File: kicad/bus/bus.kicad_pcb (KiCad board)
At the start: 2 copper layers, 45 parts, among them J1 Barrel_Jack, U29 L7805

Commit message: stuff
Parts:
- removed R12: 1k, Resistor_THT:R_Axial_DIN0207_L6.3mm_D2.5mm_P7.62mm_Horizontal
- added R14: 1k, custom_footprint_library:0.4_pitch_resistor, F.Cu at (270.5, 76.2)
- added U32: ~, custom_footprint_library:jumper, F.Cu at (133.8, 128.3)
- added U33: ~, custom_footprint_library:jumper, F.Cu at (133.8, 137.2)
- added U34: ~, Connector_PinHeader_2.54mm:PinHeader_1x07_P2.54mm_Vertical, F.Cu at (116.4, 122.4)
- R1, R10, R11, R13, R2, R3, R4, R5, R6, R7, R8, R9: footprint Resistor_THT:R_Axial_DIN0207_L6.3mm_D2.5mm_P7.62mm_Horizontal -> custom_footprint_library:0.4_pitch_resistor
- U1: footprint Connector_PinHeader_2.54mm:PinHeader_1x10_P2.54mm_Vertical -> Connector_PinHeader_2.54mm:PinHeader_1x11_P2.54mm_Vertical
- U2, U24, U3, U4, U5, U6, U7: footprint Connector_PinHeader_2.54mm:PinHeader_1x22_P2.54mm_Vertical -> Connector_PinHeader_2.54mm:PinHeader_1x23_P2.54mm_Vertical
- moved U2 152.6 mm to (259.1, 134.6), turned to 180 degrees
- moved U24 142.1 mm to (275.6, 134.6), turned to 180 degrees
- moved U3 133.1 mm to (242.6, 134.6), turned to 180 degrees
- moved U4 114.4 mm to (226.1, 134.6), turned to 180 degrees
- moved U5 96.5 mm to (209.6, 134.6), turned to 180 degrees
- moved U6 80.4 mm to (193.0, 134.6), turned to 180 degrees
- moved U7 67.0 mm to (176.5, 134.6), turned to 180 degrees
- moved R13 65.5 mm to (270.5, 109.2)
- moved R11 64.3 mm to (254.0, 76.2), turned to 180 degrees
- moved U1 48.5 mm to (102.5, 90.3)
- moved U11 48.5 mm to (112.6, 68.1)
- moved U25 48.5 mm to (108.2, 48.7)
- moved U28 48.5 mm to (119.1, 48.7)
- moved U9 48.5 mm to (64.8, 48.7)
- moved U8 48.5 mm to (54.0, 48.7)
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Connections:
- U16 pad 4: Net-(U10-GND) -> Net-(U16-2A)
- U16 pad 5: Net-(U10-GND) -> Net-(U16-2B)
- U16 pad 6: unconnected-(U16-2Q-Pad6) -> Net-(U16-2Q)
- U20 pad 1: Net-(U20-IN) -> Net-(U16-2Q)
- U21 pad 1: Net-(U19-IN) -> Net-(U21-IN)
- U28 pad 13: Net-(U19-IN) -> Net-(U21-IN)
- U30 pad 4: Net-(U10-GND) -> Net-(U21-IN)
- U30 pad 5: Net-(U10-GND) -> Net-(U16-2B)
- U30 pad 6: unconnected-(U30-2Q-Pad6) -> Net-(U19-IN)
- U31 pad 1: Net-(U20-IN) -> Net-(U16-2A)
- U31 pad 9: Net-(U19-IN) -> Net-(U21-IN)
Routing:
- net Net-(U10-GND): track 0.00 -> 203.2 mm
- net Net-(U15-D5): track 0.00 -> 128.3 mm
- net Net-(U15-D3): track 0.00 -> 128.3 mm
- net Net-(U15-D7): track 0.00 -> 128.3 mm
- net Net-(U15-D6): track 0.00 -> 128.3 mm
- net Net-(U15-D4): track 0.00 -> 128.3 mm
- net Net-(U15-D2): track 0.00 -> 128.3 mm
- net Net-(U15-D1): track 0.00 -> 128.3 mm
- net Net-(U15-D0): track 0.00 -> 128.3 mm
- net Net-(U16-2B): track 0.00 -> 99.1 mm
- net Net-(U7-FAULT): track 0.00 -> 5.08 mm
- net Net-(U4-FAULT): track 0.00 -> 5.08 mm
- net Net-(U6-FAULT): track 0.00 -> 5.08 mm
- net Net-(U3-FAULT): track 0.00 -> 5.08 mm
- net Net-(U24-FAULT): track 0.00 -> 5.08 mm
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
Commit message: Finished main PCB design
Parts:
- moved U9 122.8 mm to (187.6, 48.9), turned to 90 degrees
- moved U8 115.7 mm to (169.2, 38.1)
- moved U10 112.3 mm to (183.9, 144.8), turned to 90 degrees
- moved U25 107.3 mm to (215.0, 38.1)
- moved U13 106.3 mm to (208.0, 144.8), turned to 90 degrees
- moved U14 90.9 mm to (75.3, 139.7), turned to 180 degrees
- moved U31 90.9 mm to (75.3, 111.7), turned to 180 degrees
- moved U11 90.0 mm to (159.7, 144.8), turned to 90 degrees
- moved U33 84.0 mm to (94.9, 62.8)
- moved U32 82.9 mm to (94.9, 55.0)
- moved U34 82.6 mm to (95.2, 42.5), turned to 90 degrees
- moved U12 77.6 mm to (135.6, 144.8), turned to 90 degrees
- moved R4 69.3 mm to (119.1, 101.6)
- moved U30 62.7 mm to (67.6, 41.2)
- moved U28 56.1 mm to (75.3, 83.8), turned to 180 degrees
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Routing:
- net Net-(U10-GND): track 203.2 -> 822.5 mm
- net Net-(U10-E1): track 0.00 -> 588.7 mm, vias 0 -> 2
- net Net-(U14-0CLK): track 0.00 -> 293.3 mm, vias 0 -> 1
- net Net-(U14-1Q): track 0.00 -> 239.4 mm
- net Net-(U2-CLK_B): track 0.00 -> 218.6 mm, vias 0 -> 1
- net Net-(U12-E2#): track 0.00 -> 193.9 mm, vias 0 -> 1
- net Net-(U31-0CLK): track 0.00 -> 182.8 mm, vias 0 -> 1
- net Net-(U26-IN): track 0.00 -> 148.6 mm, vias 0 -> 2
- net Net-(U34-FAULT): track 0.00 -> 139.8 mm, vias 0 -> 1
- net Net-(U25-A0): track 0.00 -> 135.6 mm, vias 0 -> 1
- net Net-(U30-4Q): track 0.00 -> 134.9 mm
- net Net-(U10-E2#): track 0.00 -> 129.2 mm, vias 0 -> 1
- net Net-(U25-A1): track 0.00 -> 124.3 mm, vias 0 -> 1
- net Net-(U1-Start): track 0.00 -> 114.4 mm
- net Net-(U14-0D): track 0.00 -> 113.5 mm
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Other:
- board outline added: 168.7 x 126 mm
- board text added: "12V DC"
- board text added: "5V REG"
- board text added: "ARITHMETIC & LOGIC UNIT"
- board text added: "BUS READ/WRITE DECODERS"
- board text added: "CLOCK"
- board text added: "CONTROL UNIT"
- board text added: "EXTRA"
- board text added: "GENERAL-PURPOSE SRAM"
- board text added: "I/O"
- board text added: "STACK MEM CONTROLLER"
- board text added: "STARTUP CONTROLLER"

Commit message: Working on clock
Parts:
- moved R2 7.80 mm to (128.8, 105.4)
- moved R3 7.80 mm to (128.8, 72.4)
- moved R8 7.80 mm to (178.3, 105.4)
- moved R9 7.80 mm to (178.3, 72.4)
- moved U11 7.80 mm to (152.9, 148.6)
- moved U23 7.80 mm to (137.7, 54.6)
- moved U24 7.80 mm to (216.4, 130.8)
- moved U25 7.80 mm to (208.2, 41.9)
- moved U4 7.80 mm to (166.9, 130.8)
- moved U9 7.80 mm to (180.8, 52.7)
- moved U29 7.80 mm to (106.5, 129.0)
- moved U7 7.80 mm to (117.3, 130.8)
- moved U1 7.80 mm to (117.3, 133.4)
- moved U14 7.80 mm to (68.5, 143.5)
- moved U15 7.80 mm to (107.8, 100.3)
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
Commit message: Designed sample board
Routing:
- added copper zone on B.Cu, net Net-(U10-GND)
- added copper zone on F.Cu, net Net-(U10-GND)
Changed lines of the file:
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@@
 		(net 149)
+	)
+	(zone
+		(net 2)
+		(net_name "Net-(U10-GND)")
+		(layers "F&B.Cu")
+		(name "gnd-fill")
+		(hatch edge 0.5)
+		(connect_pads yes
+			(clearance 0.5)
+		)
+		(min_thickness 0.25)
+		(filled_areas_thickness no)
+		(fill yes
+			(thermal_gap 0.5)
+			(thermal_bridge_width 0.5)
+		)
+		(polygon
+			(pts
+				(xy 56.134 36.576) (xy 56.134 161.036) (xy 223.266 161.036) (xy 223.266 36.576)
+			)
+		)
 	)
 	(group ""

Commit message: Done w/ ALU schematic
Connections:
- U13 pad 9: unconnected-(U13-Y6-Pad9) -> Net-(U13-Y6)
- U6 pad 3: unconnected-(U6-READ_2-Pad3) -> Net-(U13-Y6)
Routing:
- net Net-(U13-Y6): track 0.00 -> 101.3 mm, vias 0 -> 4

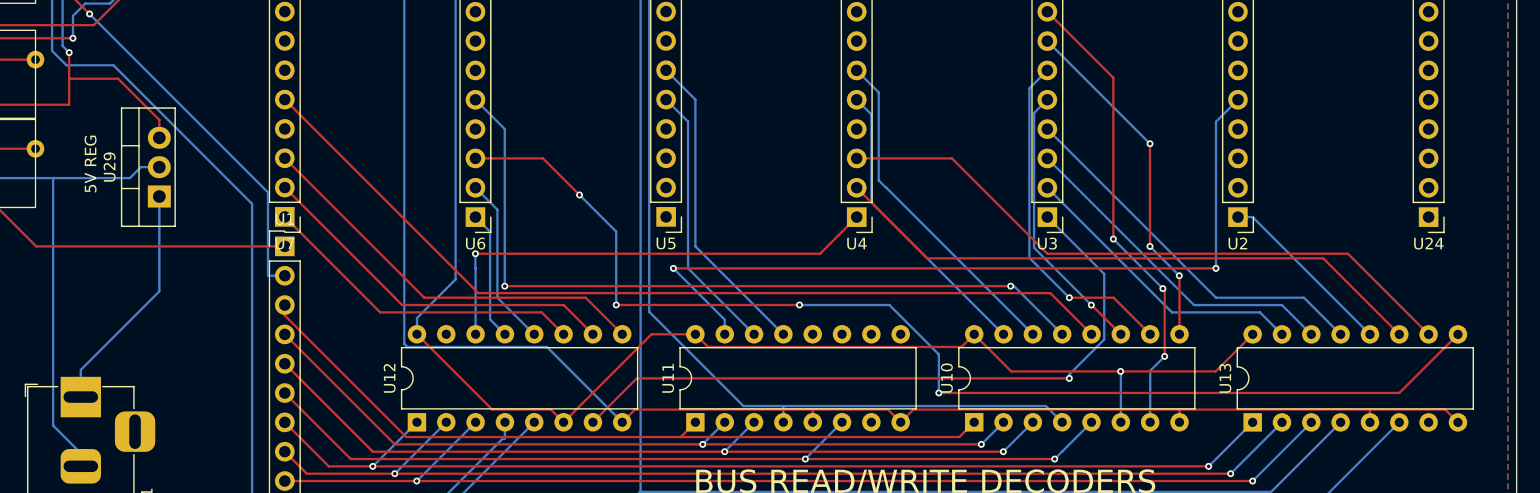
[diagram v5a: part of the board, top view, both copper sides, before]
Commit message: Finished IO controller schematic
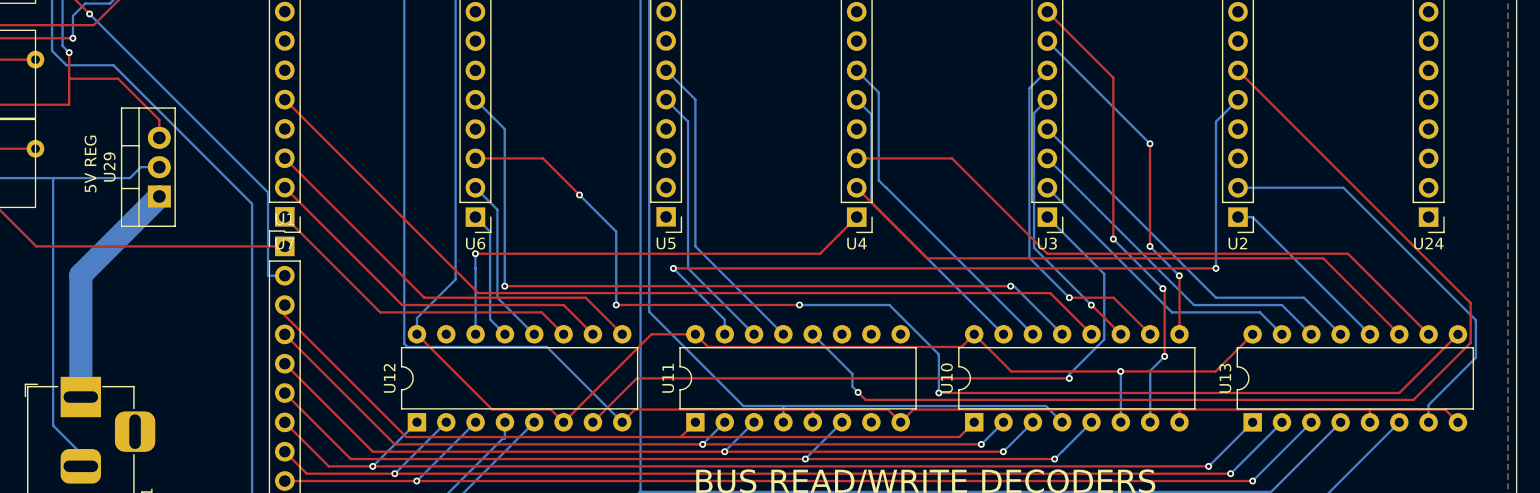
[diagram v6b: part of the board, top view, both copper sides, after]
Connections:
- U11 pad 12: unconnected-(U11-Y3-Pad12) -> Net-(U11-Y3)
- U13 pad 7: unconnected-(U13-Y7-Pad7) -> Net-(U13-Y7)
- U2 pad 2: unconnected-(U2-READ_1-Pad2) -> Net-(U13-Y7)
- U2 pad 6: unconnected-(U2-WRITE_1-Pad6) -> Net-(U11-Y3)
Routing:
- net Net-(U11-Y3): track 0.00 -> 94.0 mm, vias 0 -> 1
- net Net-(U13-Y7): track 0.00 -> 35.9 mm
- added copper zone on F.Cu, net Net-(U10-E1)
- removed copper zone on F.Cu, net Net-(U10-GND)

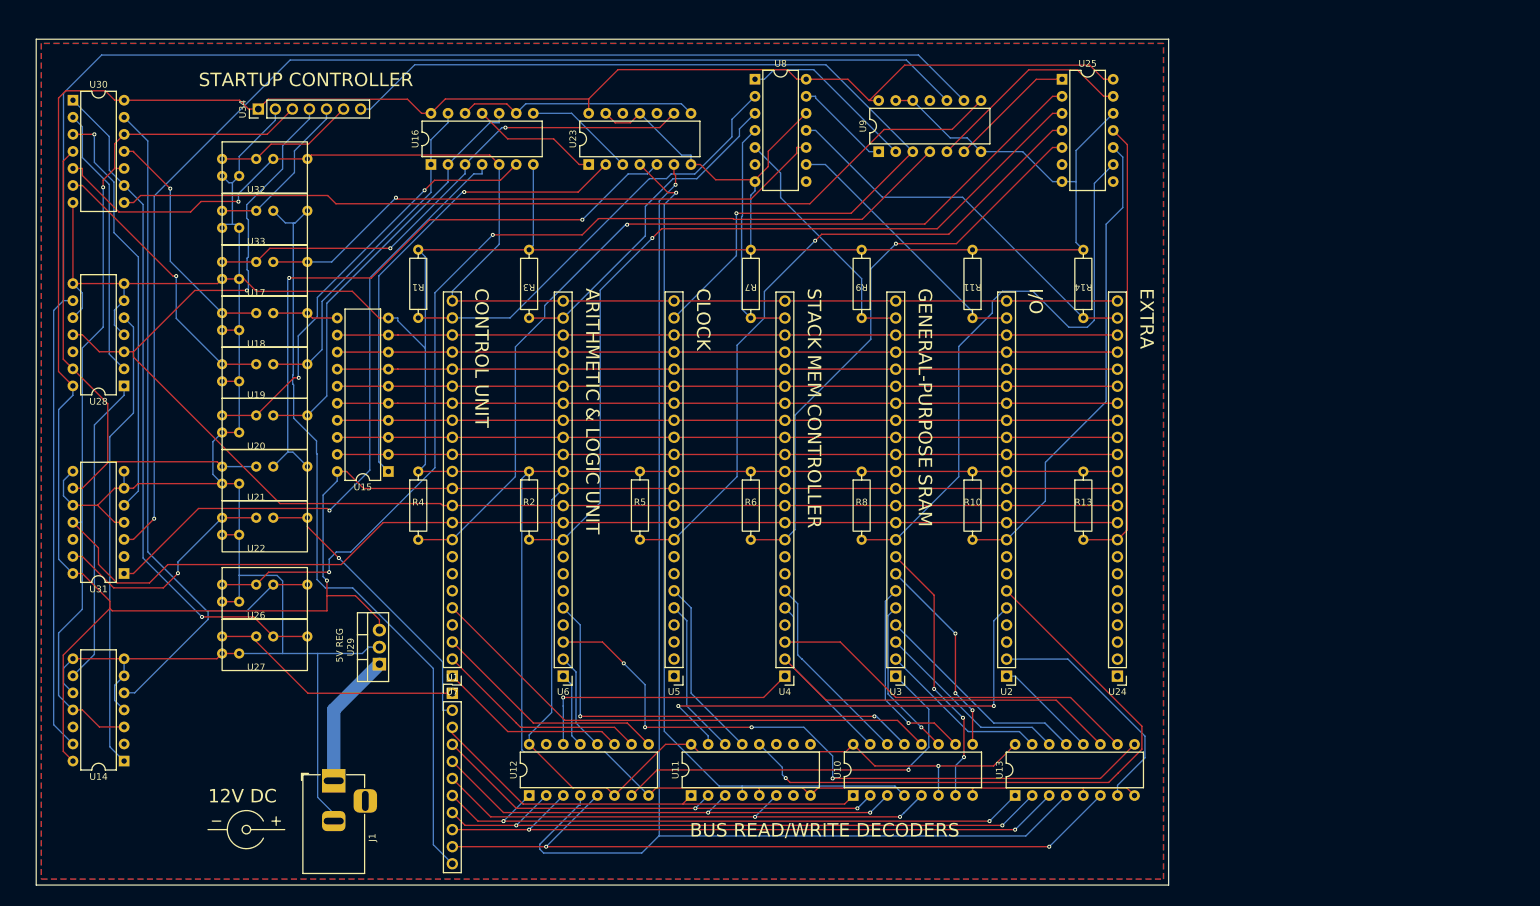
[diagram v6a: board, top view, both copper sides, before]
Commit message: Finished some more PCBs and uploaded to JLCPCB
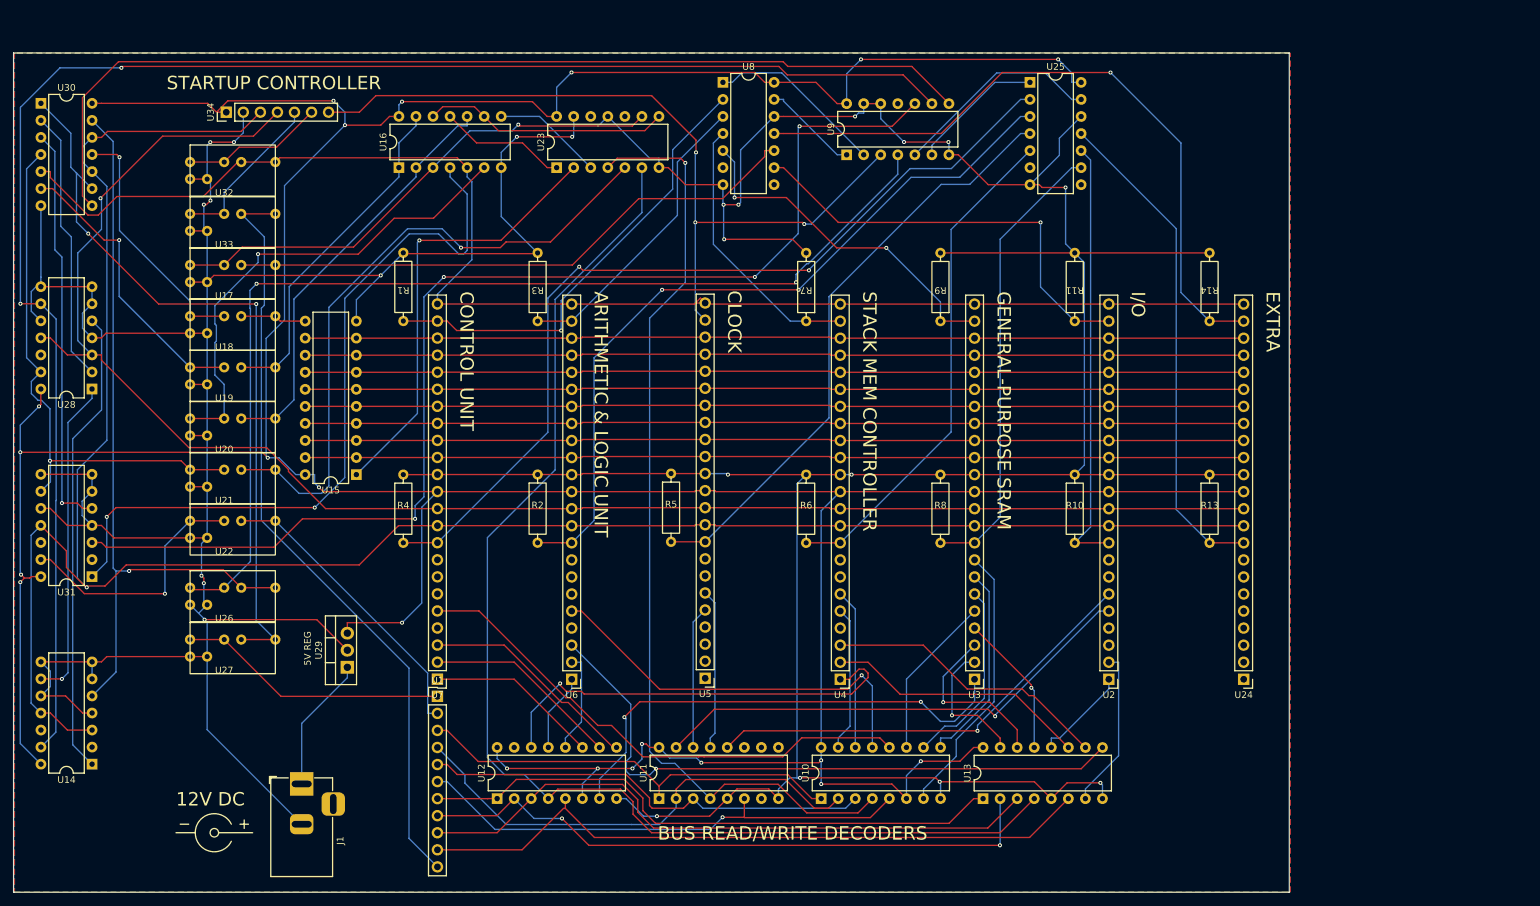
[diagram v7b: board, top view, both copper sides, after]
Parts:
- moved U24 18.8 mm to (235.2, 131.3)
- moved R13 18.8 mm to (230.1, 105.9)
- moved R14 18.8 mm to (230.1, 72.9)
- moved U2 15.2 mm to (215.1, 131.3)
- moved R11 15.2 mm to (210.0, 72.9)
- moved R10 15.2 mm to (210.0, 105.9)
- moved R8 11.7 mm to (190.0, 105.9)
- moved R9 11.7 mm to (190.0, 72.9)
- moved U3 11.7 mm to (195.1, 131.3)
- moved U4 8.26 mm to (175.1, 131.3)
- moved R6 8.26 mm to (170.0, 105.9)
- moved R7 8.26 mm to (170.0, 72.9)
- moved J1 4.80 mm to (94.9, 146.9)
- moved U12 4.80 mm to (124.0, 149.1)
- moved U17 4.80 mm to (83.4, 74.7)
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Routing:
- net Net-(U10-E1): track 588.7 -> 638.6 mm, vias 2 -> 21
- net Net-(U24-FAULT): track 57.9 -> 102.1 mm, vias 0 -> 1
- net Net-(U10-GND): track 822.5 -> 862.0 mm, vias 0 -> 23
- net Net-(U14-0CLK): track 293.3 -> 324.3 mm
- net Net-(U2-CLK_B): track 218.6 -> 247.9 mm
- net Net-(U11-Y3): track 94.0 -> 66.8 mm
- net Net-(U2-FAULT): track 39.9 -> 65.0 mm, vias 0 -> 1
- net Net-(U15-D4): track 116.2 -> 139.9 mm
- net Net-(U15-D6): track 116.3 -> 139.9 mm
- net Net-(U15-D3): track 116.3 -> 139.9 mm
- net Net-(U15-D7): track 116.3 -> 139.9 mm
- net Net-(U15-D5): track 116.3 -> 139.9 mm
- net Net-(U12-Y1): track 41.3 -> 64.8 mm
- net Net-(U15-D1): track 116.9 -> 139.9 mm
- net Net-(U15-D0): track 116.9 -> 139.9 mm
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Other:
- board size 168.7 x 126 mm -> 190 x 125 mm
